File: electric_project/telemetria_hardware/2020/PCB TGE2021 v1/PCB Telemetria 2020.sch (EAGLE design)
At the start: 22 parts, among them IC1 INA240A1DR, IC2 MCP3221A6T-E_OTVAO, IC3 AZ1117IH-3.3TRG1, IC4 ACS758LCB-050B-PFF-T

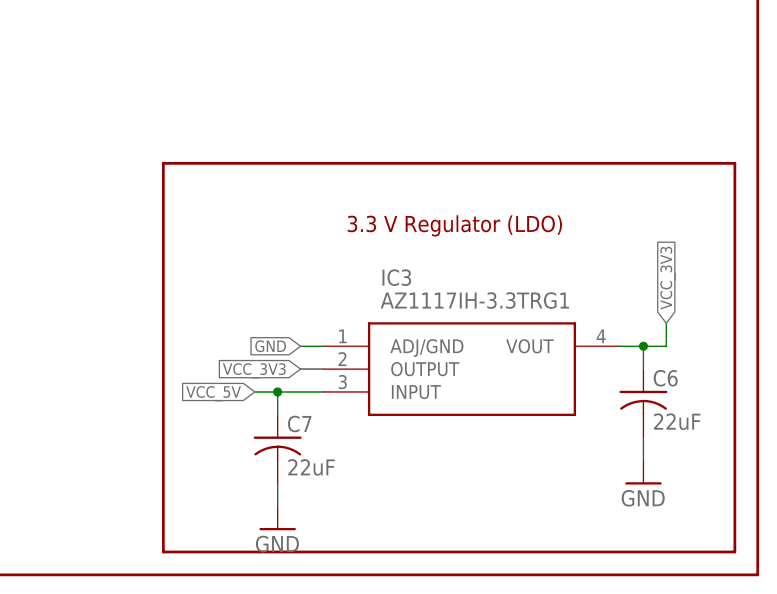
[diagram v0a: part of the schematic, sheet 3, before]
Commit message: Position updates to the board.
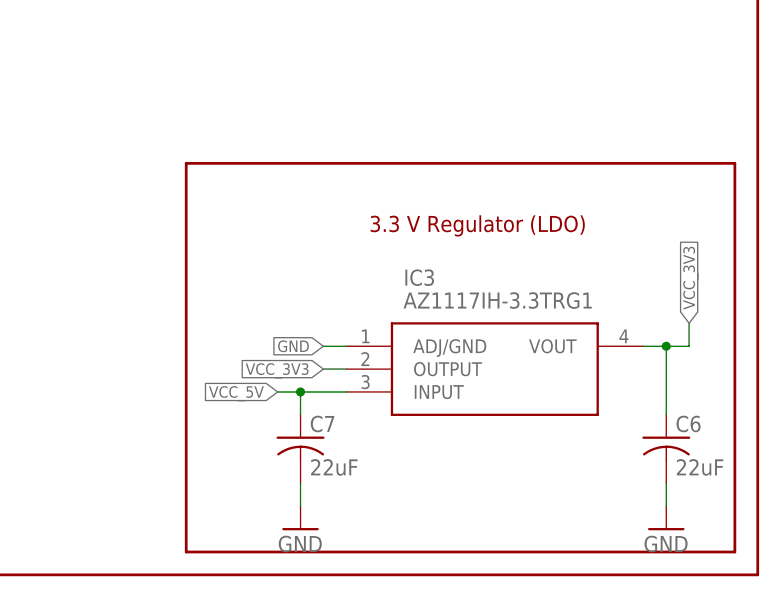
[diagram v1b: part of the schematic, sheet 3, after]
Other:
- moved on the sheet: C6, C7, IC3
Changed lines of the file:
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@@
 <wire x1="106.68" y1="198.12" x2="106.68" y2="233.68" width="0.1524" layer="94"/>
 <wire x1="106.68" y1="233.68" x2="15.24" y2="233.68" width="0.1524" layer="94"/>
-<text x="43.18" y="228.6" size="1.778" layer="94">Motor Current Sense Amplifier</text>
+<text x="45.72" y="228.6" size="1.778" layer="94">Motor Current Sense Amplifier</text>
 <wire x1="15.24" y1="195.58" x2="15.24" y2="157.48" width="0.1524" layer="94"/>
 <wire x1="15.24" y1="157.48" x2="106.68" y2="157.48" width="0.1524" layer="94"/>
@@
 <wire x1="276.86" y1="182.88" x2="276.86" y2="248.92" width="0.3048" layer="94"/>
 <wire x1="276.86" y1="248.92" x2="149.86" y2="248.92" width="0.3048" layer="94"/>
-<wire x1="210.82" y1="228.6" x2="210.82" y2="185.42" width="0.3048" layer="94"/>
-<wire x1="210.82" y1="185.42" x2="274.32" y2="185.42" width="0.3048" layer="94"/>
+<wire x1="213.36" y1="228.6" x2="213.36" y2="185.42" width="0.3048" layer="94"/>
+<wire x1="213.36" y1="185.42" x2="274.32" y2="185.42" width="0.3048" layer="94"/>
 <wire x1="274.32" y1="185.42" x2="274.32" y2="228.6" width="0.3048" layer="94"/>
-<wire x1="274.32" y1="228.6" x2="210.82" y2="228.6" width="0.3048" layer="94"/>
-<text x="231.14" y="220.98" size="1.778" layer="94">3.3 V Regulator (LDO)</text>
+<wire x1="274.32" y1="228.6" x2="213.36" y2="228.6" width="0.3048" layer="94"/>
+<text x="233.68" y="220.98" size="1.778" layer="94">3.3 V Regulator (LDO)</text>
 </plain>
 <instances>
@@
 <attribute name="VALUE" x="20.32" y="209.55" size="1.778" layer="96" rot="R90" align="center-left"/>
 </instance>
-<instance part="IC3" gate="G$1" x="228.6" y="208.28" smashed="yes">
-<attribute name="NAME" x="234.95" y="215.9" size="1.778" layer="95" align="center-left"/>
-<attribute name="VALUE" x="234.95" y="213.36" size="1.778" layer="96" align="center-left"/>
-</instance>
-<instance part="C6" gate="G$1" x="264.16" y="203.2" smashed="yes">
-<attribute name="NAME" x="265.176" y="203.835" size="1.778" layer="95"/>
-<attribute name="VALUE" x="265.176" y="199.009" size="1.778" layer="96"/>
-</instance>
-<instance part="GND4" gate="1" x="264.16" y="193.04" smashed="yes">
-<attribute name="VALUE" x="261.62" y="190.5" size="1.778" layer="96"/>
-</instance>
-<instance part="C7" gate="G$1" x="223.52" y="198.12" smashed="yes">
-<attribute name="NAME" x="224.536" y="198.755" size="1.778" layer="95"/>
-<attribute name="VALUE" x="224.536" y="193.929" size="1.778" layer="96"/>
-</instance>
-<instance part="GND5" gate="1" x="223.52" y="187.96" smashed="yes">
-<attribute name="VALUE" x="220.98" y="185.42" size="1.778" layer="96"/>
+<instance part="IC3" gate="G$1" x="231.14" y="208.28" smashed="yes">
+<attribute name="NAME" x="237.49" y="215.9" size="1.778" layer="95" align="center-left"/>
+<attribute name="VALUE" x="237.49" y="213.36" size="1.778" layer="96" align="center-left"/>
+</instance>
+<instance part="C6" gate="G$1" x="266.7" y="198.12" smashed="yes">
+<attribute name="NAME" x="267.716" y="198.755" size="1.778" layer="95"/>
+<attribute name="VALUE" x="267.716" y="193.929" size="1.778" layer="96"/>
+</instance>
+<instance part="GND4" gate="1" x="266.7" y="187.96" smashed="yes">
+<attribute name="VALUE" x="264.16" y="185.42" size="1.778" layer="96"/>
+</instance>
+<instance part="C7" gate="G$1" x="226.06" y="198.12" smashed="yes">
+<attribute name="NAME" x="227.076" y="198.755" size="1.778" layer="95"/>
+<attribute name="VALUE" x="227.076" y="193.929" size="1.778" layer="96"/>
+</instance>
+<instance part="GND5" gate="1" x="226.06" y="187.96" smashed="yes">
+<attribute name="VALUE" x="223.52" y="185.42" size="1.778" layer="96"/>
 </instance>
 </instances>
@@
 <segment>
 <pinref part="IC3" gate="G$1" pin="ADJ/GND"/>
-<wire x1="228.6" y1="208.28" x2="226.06" y2="208.28" width="0.1524" layer="91"/>
-<label x="226.06" y="208.28" size="1.27" layer="95" rot="R180" xref="yes"/>
+<wire x1="231.14" y1="208.28" x2="228.6" y2="208.28" width="0.1524" layer="91"/>
+<label x="228.6" y="208.28" size="1.27" layer="95" rot="R180" xref="yes"/>
 </segment>
 <segment>
 <pinref part="GND4" gate="1" pin="GND"/>
 <pinref part="C6" gate="G$1" pin="2"/>
-<wire x1="264.16" y1="195.58" x2="264.16" y2="198.12" width="0.1524" layer="91"/>
+<wire x1="266.7" y1="190.5" x2="266.7" y2="193.04" width="0.1524" layer="91"/>
 </segment>
 <segment>
 <pinref part="GND5" gate="1" pin="GND"/>
 <pinref part="C7" gate="G$1" pin="2"/>
-<wire x1="223.52" y1="190.5" x2="223.52" y2="193.04" width="0.1524" layer="91"/>
+<wire x1="226.06" y1="190.5" x2="226.06" y2="193.04" width="0.1524" layer="91"/>
 </segment>
 </net>
@@
 <segment>
 <pinref part="IC3" gate="G$1" pin="INPUT"/>
-<wire x1="228.6" y1="203.2" x2="223.52" y2="203.2" width="0.1524" layer="91"/>
-<label x="220.98" y="203.2" size="1.27" layer="95" rot="R180" xref="yes"/>
+<wire x1="231.14" y1="203.2" x2="226.06" y2="203.2" width="0.1524" layer="91"/>
+<label x="223.52" y="203.2" size="1.27" layer="95" rot="R180" xref="yes"/>
 <pinref part="C7" gate="G$1" pin="1"/>
-<wire x1="223.52" y1="203.2" x2="220.98" y2="203.2" width="0.1524" layer="91"/>
-<wire x1="223.52" y1="200.66" x2="223.52" y2="203.2" width="0.1524" layer="91"/>
-<junction x="223.52" y="203.2"/>
+<wire x1="226.06" y1="203.2" x2="223.52" y2="203.2" width="0.1524" layer="91"/>
+<wire x1="226.06" y1="200.66" x2="226.06" y2="203.2" width="0.1524" layer="91"/>
+<junction x="226.06" y="203.2"/>
 </segment>
 </net>
@@
 <segment>
 <pinref part="IC3" gate="G$1" pin="VOUT"/>
-<wire x1="261.62" y1="208.28" x2="264.16" y2="208.28" width="0.1524" layer="91"/>
-<label x="266.7" y="210.82" size="1.27" layer="95" rot="R90" xref="yes"/>
+<wire x1="264.16" y1="208.28" x2="266.7" y2="208.28" width="0.1524" layer="91"/>
+<label x="269.24" y="210.82" size="1.27" layer="95" rot="R90" xref="yes"/>
 <pinref part="C6" gate="G$1" pin="1"/>
-<wire x1="264.16" y1="205.74" x2="264.16" y2="208.28" width="0.1524" layer="91"/>
-<wire x1="264.16" y1="208.28" x2="266.7" y2="208.28" width="0.1524" layer="91"/>
-<junction x="264.16" y="208.28"/>
-<wire x1="266.7" y1="208.28" x2="266.7" y2="210.82" width="0.1524" layer="91"/>
+<wire x1="266.7" y1="200.66" x2="266.7" y2="208.28" width="0.1524" layer="91"/>
+<wire x1="266.7" y1="208.28" x2="269.24" y2="208.28" width="0.1524" layer="91"/>
+<junction x="266.7" y="208.28"/>
+<wire x1="269.24" y1="208.28" x2="269.24" y2="210.82" width="0.1524" layer="91"/>
 </segment>
 <segment>
 <pinref part="IC3" gate="G$1" pin="OUTPUT"/>
-<wire x1="228.6" y1="205.74" x2="226.06" y2="205.74" width="0.1524" layer="91"/>
-<label x="226.06" y="205.74" size="1.27" layer="95" rot="R180" xref="yes"/>
-</segment>
-</net>
+<wire x1="231.14" y1="205.74" x2="228.6" y2="205.74" width="0.1524" layer="91"/>
+<label x="228.6" y="205.74" size="1.27" layer="95" rot="R180" xref="yes"/>
+</segment>
+</net>

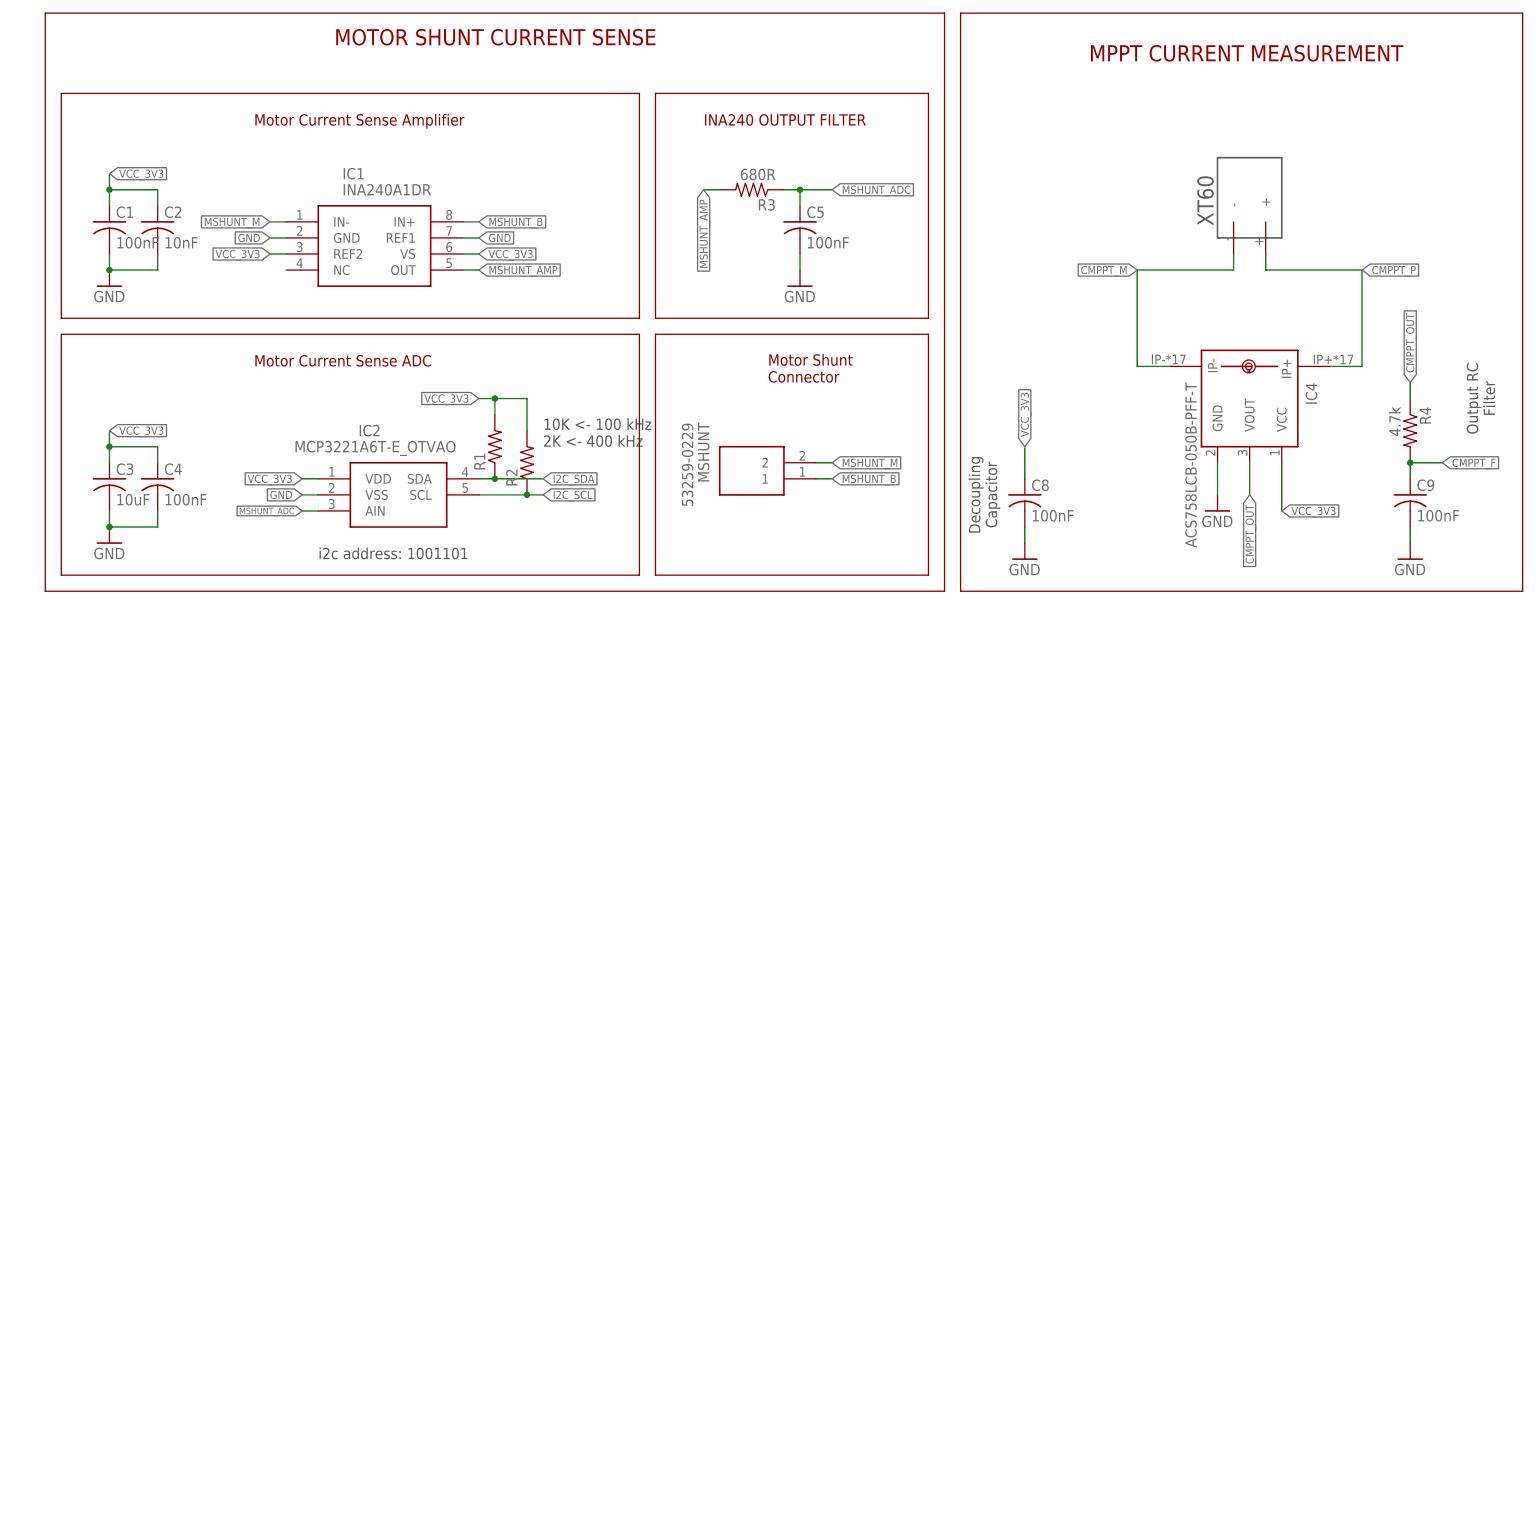
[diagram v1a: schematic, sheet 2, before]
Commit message: Adding ADS1115 and BBank input circuit
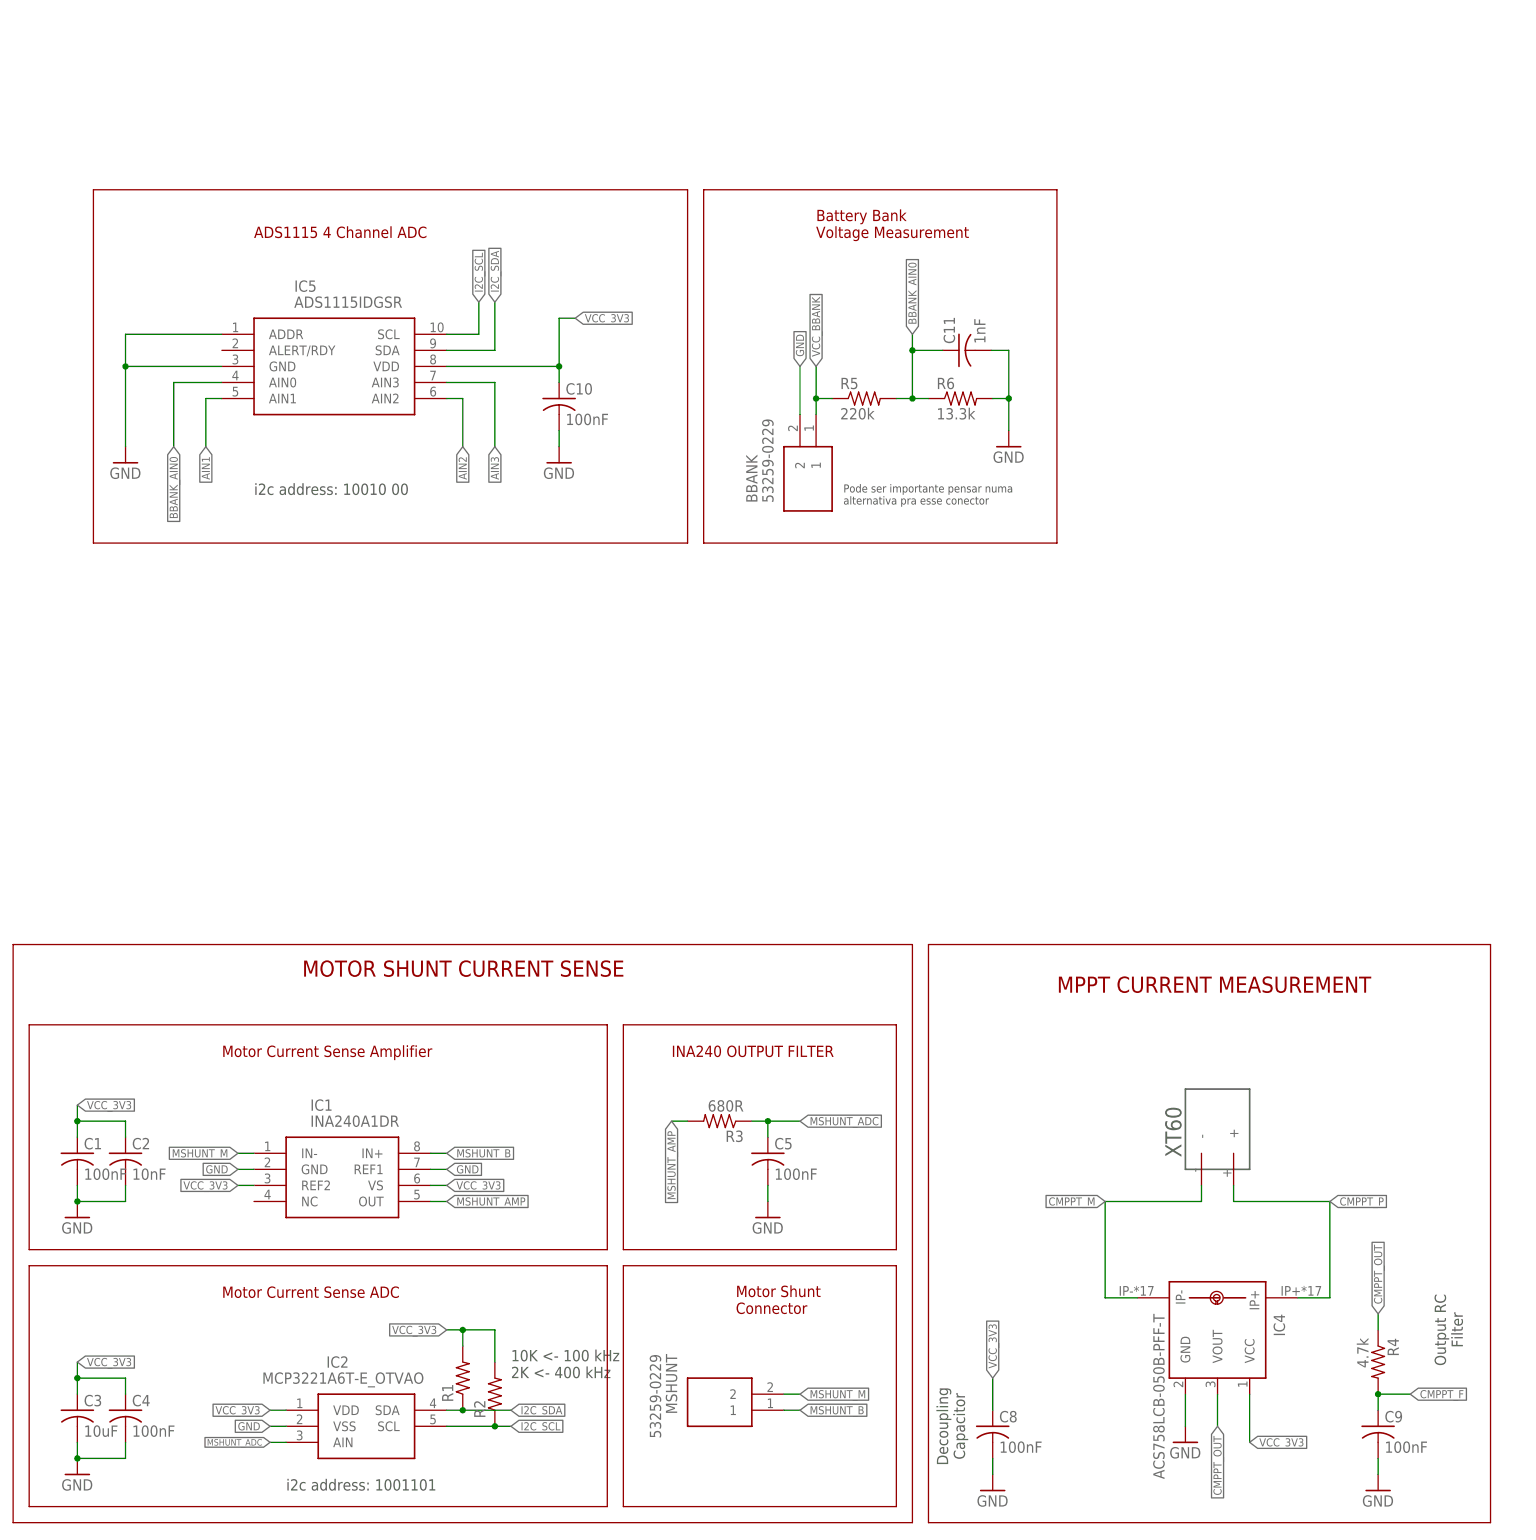
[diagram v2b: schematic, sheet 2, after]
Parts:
- added BBANK: 53259-0229, CON_MOLEX_53259-0229:53259-0229
- added C10: 100nF, rcl:C-USC0805
- added C11: 1nF, rcl:C-USC0805
- added IC5: ADS1115IDGSR, SamacSys_Parts:ADS1115IDGSR
- added R5: 220k, rcl:R-US_R0805
- added R6: 13.3k, rcl:R-US_R0805
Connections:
- new net AIN1: IC5.AIN1
- new net AIN2: IC5.AIN2
- new net AIN3: IC5.AIN3
- new net BBANK_AIN0: C11.1, IC5.AIN0, R5.2, R6.1
- new net VCC_BBANK: BBANK.1, R5.1
- net GND: now also BBANK.2, C10.2, C11.2, IC5.ADDR, IC5.GND, R6.2
- net I2C_SCL: now also IC5.SCL
- net I2C_SDA: now also IC5.SDA
- net VCC_3V3: now also C10.1, IC5.VDD
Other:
- note added: "ADS1115 4 Channel ADC"
- note added: "Battery Bank Voltage Measurement"
- note added: "Pode ser importante pensar numa alternativa pra esse conector"
- note added: "i2c address: 10010 00"
- moved on the sheet: C1, C2, C3, C4, C5, C8, C9, IC1, IC2, IC4, MSHUNT, R1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

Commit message: Adding the initial sch. of the PV voltage measurement circuit
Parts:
- added C12: (no value), rcl:C-USC0805
- added R7, R8: (no value), rcl:R-US_R0805
- added VPV: 53259-0229, CON_MOLEX_53259-0229:53259-0229
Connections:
- removed net AIN1: IC5.AIN1
- new net PV_AIN1: C12.1, IC5.AIN1, R7.2, R8.1
- new net VCC_PV: R7.1, VPV.1
- net GND: now also C12.2, R8.2, VPV.2
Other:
- moved on the sheet: BBANK, C11, R5, R6
